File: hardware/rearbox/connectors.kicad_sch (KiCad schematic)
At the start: 2 parts, among them J3 Conn_02x28_Top_Bottom, J4 Auxiliary

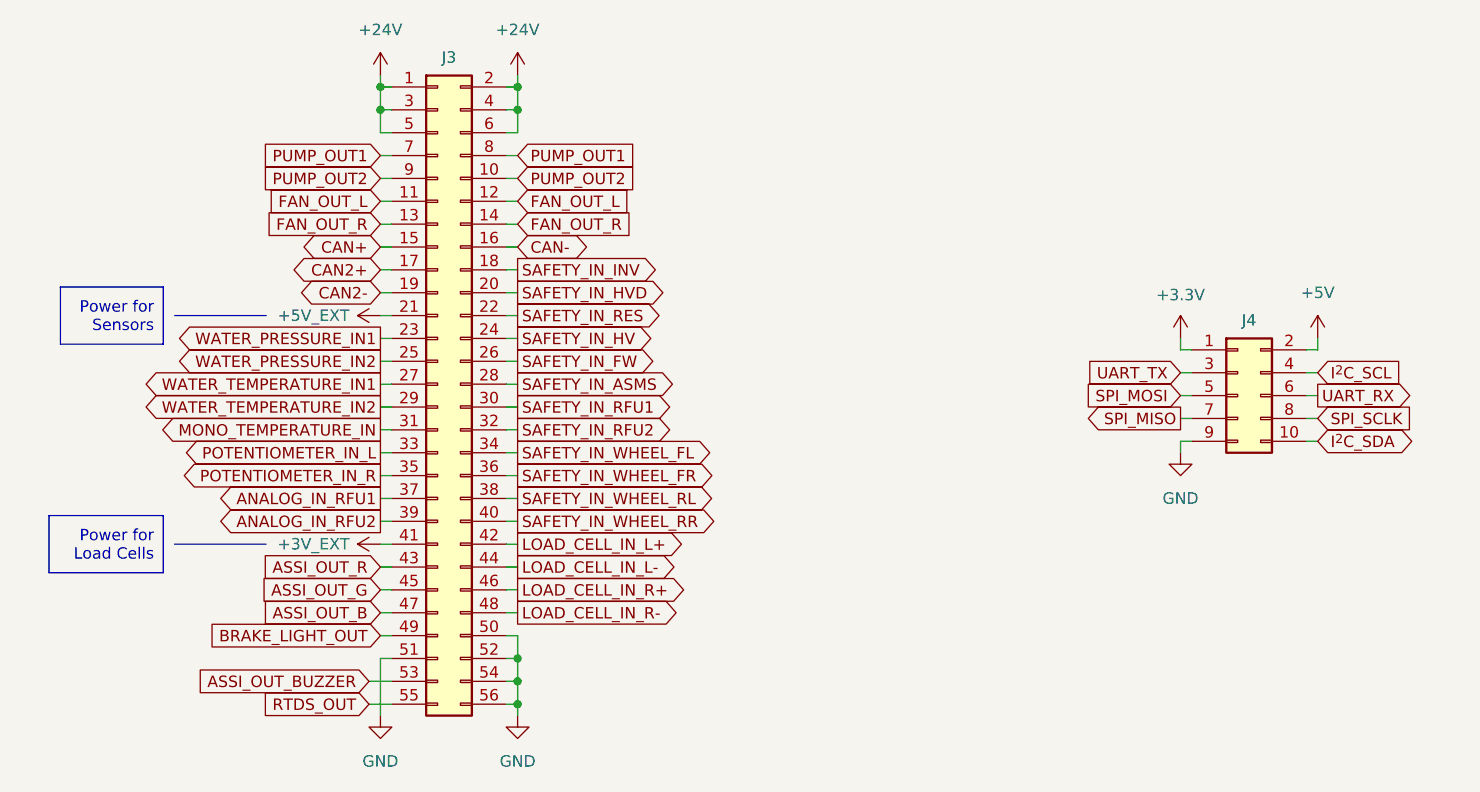
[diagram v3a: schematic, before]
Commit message: Route PCB tracks
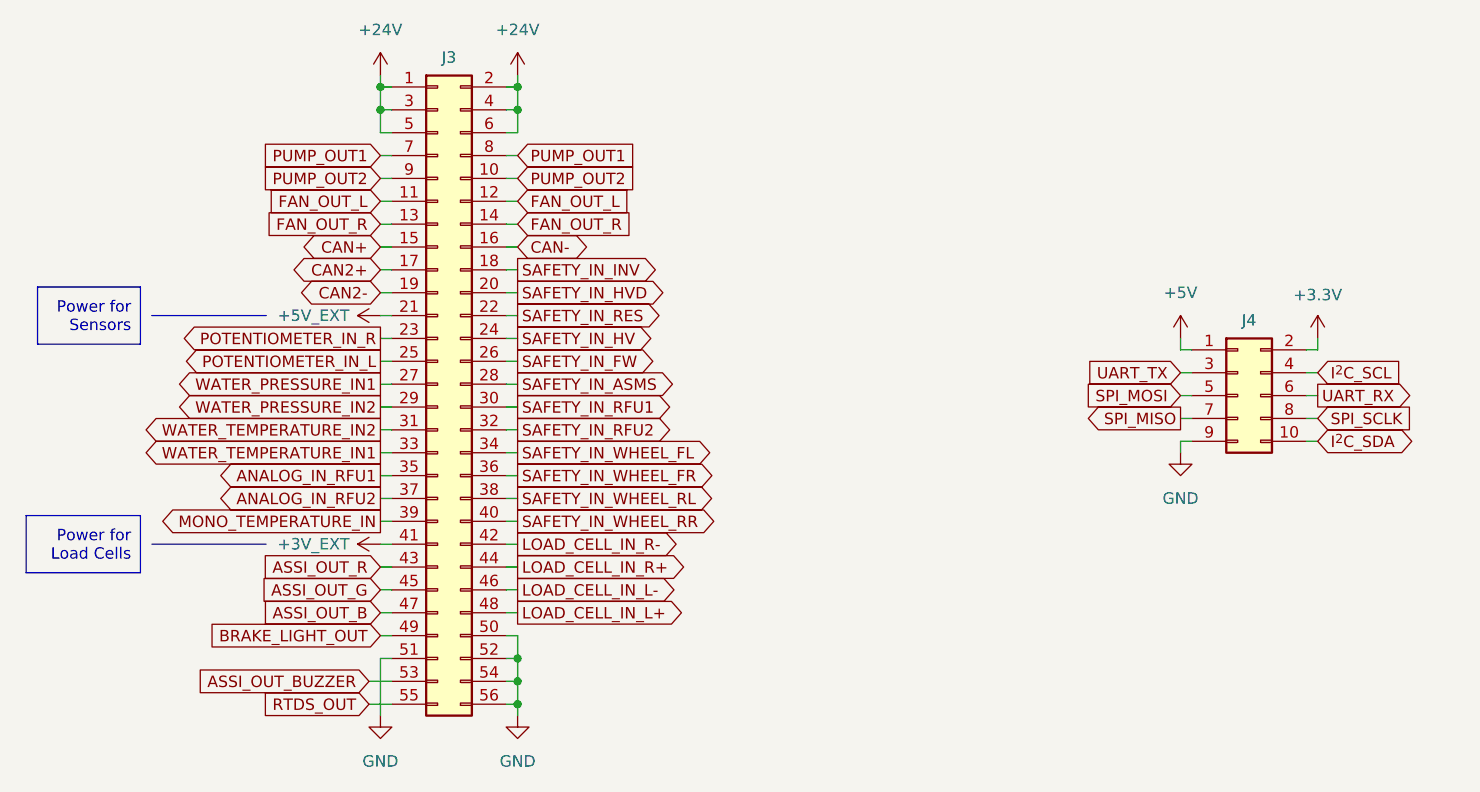
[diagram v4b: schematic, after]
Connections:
- net +3.3V: now also J4.2 (Pin_2); no longer J4.1 (Pin_1)
- net +5V: now also J4.1 (Pin_1); no longer J4.2 (Pin_2)
- net ANALOG_IN_RFU1: now also J3.35 (Pin_35); no longer J3.37 (Pin_37)
- net ANALOG_IN_RFU2: now also J3.37 (Pin_37); no longer J3.39 (Pin_39)
- net LOAD_CELL_IN_L+: now also J3.48 (Pin_48); no longer J3.42 (Pin_42)
- net LOAD_CELL_IN_L-: now also J3.46 (Pin_46); no longer J3.44 (Pin_44)
- net LOAD_CELL_IN_R+: now also J3.44 (Pin_44); no longer J3.46 (Pin_46)
- net LOAD_CELL_IN_R-: now also J3.42 (Pin_42); no longer J3.48 (Pin_48)
- net MONO_TEMPERATURE_IN: now also J3.39 (Pin_39); no longer J3.31 (Pin_31)
- net POTENTIOMETER_IN_L: now also J3.25 (Pin_25); no longer J3.33 (Pin_33)
- net POTENTIOMETER_IN_R: now also J3.23 (Pin_23); no longer J3.35 (Pin_35)
- net WATER_PRESSURE_IN1: now also J3.27 (Pin_27); no longer J3.23 (Pin_23)
- net WATER_PRESSURE_IN2: now also J3.29 (Pin_29); no longer J3.25 (Pin_25)
- net WATER_TEMPERATURE_IN1: now also J3.33 (Pin_33); no longer J3.27 (Pin_27)
- net WATER_TEMPERATURE_IN2: now also J3.31 (Pin_31); no longer J3.29 (Pin_29)
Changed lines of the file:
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@@
     (stroke (width 0) (type default))
   )
-  (polyline (pts (xy 93.98 91.44) (xy 83.82 91.44))
+  (polyline (pts (xy 93.98 91.44) (xy 81.28 91.44))
     (stroke (width 0) (type default))
   )
@@
     (stroke (width 0) (type default))
   )
-  (polyline (pts (xy 93.98 116.84) (xy 83.82 116.84))
+  (polyline (pts (xy 93.98 116.84) (xy 81.28 116.84))
     (stroke (width 0) (type default))
   )
@@
   )
   (text_box "Power for Sensors"
-    (at 71.12 88.265 0) (size 11.43 6.35)
+    (at 68.58 88.265 0) (size 11.43 6.35)
     (stroke (width 0) (type default))
     (fill (type none))
@@
   )
   (text_box "Power for Load Cells"
-    (at 69.85 113.665 0) (size 12.7 6.35)
+    (at 67.31 113.665 0) (size 12.7 6.35)
     (stroke (width 0) (type default))
     (fill (type none))
     (effects (font (size 1.27 1.27)) (justify right))
   )
-  (global_label "WATER_PRESSURE_IN1" (shape output) (at 106.68 93.98 180) (fields_autoplaced)
+  (global_label "WATER_PRESSURE_IN1" (shape output) (at 106.68 99.06 180) (fields_autoplaced)
     (effects (font (size 1.27 1.27) (color 0 132 132 1)) (justify right))
-    (property "Intersheetrefs" "${INTERSHEET_REFS}" (at 82.9101 93.98 0)
+    (property "Intersheetrefs" "${INTERSHEET_REFS}" (at 82.9101 99.06 0)
       (effects (font (size 1.27 1.27)) (justify right) hide)
     )
@@
     )
   )
-  (global_label "WATER_PRESSURE_IN2" (shape output) (at 106.68 96.52 180) (fields_autoplaced)
+  (global_label "WATER_PRESSURE_IN2" (shape output) (at 106.68 101.6 180) (fields_autoplaced)
     (effects (font (size 1.27 1.27) (color 0 132 132 1)) (justify right))
-    (property "Intersheetrefs" "${INTERSHEET_REFS}" (at 82.9101 96.52 0)
+    (property "Intersheetrefs" "${INTERSHEET_REFS}" (at 82.9101 101.6 0)
       (effects (font (size 1.27 1.27)) (justify right) hide)
     )
@@
     )
   )
-  (global_label "WATER_TEMPERATURE_IN1" (shape output) (at 106.68 99.06 180) (fields_autoplaced)
+  (global_label "WATER_TEMPERATURE_IN1" (shape output) (at 106.68 106.68 180) (fields_autoplaced)
     (effects (font (size 1.27 1.27) (color 0 255 255 1)) (justify right))
-    (property "Intersheetrefs" "${INTERSHEET_REFS}" (at 79.7049 99.06 0)
+    (property "Intersheetrefs" "${INTERSHEET_REFS}" (at 79.7049 106.68 0)
       (effects (font (size 1.27 1.27)) (justify right) hide)
     )
@@
     )
   )
-  (global_label "LOAD_CELL_IN_R+" (shape output) (at 121.92 121.92 0) (fields_autoplaced)
+  (global_label "LOAD_CELL_IN_R+" (shape output) (at 121.92 119.38 0) (fields_autoplaced)
     (effects (font (size 1.27 1.27)) (justify left))
-    (property "Intersheetrefs" "${INTERSHEET_REFS}" (at 141.7781 121.92 0)
+    (property "Intersheetrefs" "${INTERSHEET_REFS}" (at 141.7781 119.38 0)
       (effects (font (size 1.27 1.27)) (justify left) hide)
     )
@@
     )
   )
-  (global_label "LOAD_CELL_IN_R-" (shape output) (at 121.92 124.46 0) (fields_autoplaced)
+  (global_label "LOAD_CELL_IN_R-" (shape output) (at 121.92 116.84 0) (fields_autoplaced)
     (effects (font (size 1.27 1.27)) (justify left))
-    (property "Intersheetrefs" "${INTERSHEET_REFS}" (at 141.7781 124.46 0)
-      (effects (font (size 1.27 1.27)) (justify left) hide)
-    )
-  )
-  (global_label "LOAD_CELL_IN_L+" (shape output) (at 121.92 116.84 0) (fields_autoplaced)
+    (property "Intersheetrefs" "${INTERSHEET_REFS}" (at 141.7781 116.84 0)
+      (effects (font (size 1.27 1.27)) (justify left) hide)
+    )
+  )
+  (global_label "LOAD_CELL_IN_L+" (shape output) (at 121.92 124.46 0) (fields_autoplaced)
     (effects (font (size 1.27 1.27)) (justify left))
-    (property "Intersheetrefs" "${INTERSHEET_REFS}" (at 141.5362 116.84 0)
+    (property "Intersheetrefs" "${INTERSHEET_REFS}" (at 141.5362 124.46 0)
       (effects (font (size 1.27 1.27)) (justify left) hide)
     )
@@
     )
   )
-  (global_label "MONO_TEMPERATURE_IN" (shape output) (at 106.68 104.14 180) (fields_autoplaced)
+  (global_label "MONO_TEMPERATURE_IN" (shape output) (at 106.68 114.3 180) (fields_autoplaced)
     (effects (font (size 1.27 1.27) (color 0 255 255 1)) (justify right))
-    (property "Intersheetrefs" "${INTERSHEET_REFS}" (at 81.3981 104.14 0)
+    (property "Intersheetrefs" "${INTERSHEET_REFS}" (at 81.3981 114.3 0)
       (effects (font (size 1.27 1.27)) (justify right) hide)
     )
@@
     )
   )
-  (global_label "ANALOG_IN_RFU2" (shape output) (at 106.68 114.3 180) (fields_autoplaced)
+  (global_label "ANALOG_IN_RFU2" (shape output) (at 106.68 111.76 180) (fields_autoplaced)
     (effects (font (size 1.27 1.27)) (justify right))
-    (property "Intersheetrefs" "${INTERSHEET_REFS}" (at 87.7894 114.3 0)
+    (property "Intersheetrefs" "${INTERSHEET_REFS}" (at 87.7894 111.76 0)
       (effects (font (size 1.27 1.27)) (justify right) hide)
     )
@@
     )
   )
-  (global_label "LOAD_CELL_IN_L-" (shape output) (at 121.92 119.38 0) (fields_autoplaced)
+  (global_label "LOAD_CELL_IN_L-" (shape output) (at 121.92 121.92 0) (fields_autoplaced)
     (effects (font (size 1.27 1.27)) (justify left))
-    (property "Intersheetrefs" "${INTERSHEET_REFS}" (at 141.5362 119.38 0)
+    (property "Intersheetrefs" "${INTERSHEET_REFS}" (at 141.5362 121.92 0)
       (effects (font (size 1.27 1.27)) (justify left) hide)
     )
@@
     )
   )
-  (global_label "POTENTIOMETER_IN_R" (shape output) (at 106.68 109.22 180) (fields_autoplaced)
+  (global_label "POTENTIOMETER_IN_R" (shape output) (at 106.68 93.98 180) (fields_autoplaced)
     (effects (font (size 1.27 1.27)) (justify right))
-    (property "Intersheetrefs" "${INTERSHEET_REFS}" (at 83.6168 109.22 0)
-      (effects (font (size 1.27 1.27)) (justify right) hide)
-    )
-  )
-  (global_label "ANALOG_IN_RFU1" (shape output) (at 106.68 111.76 180) (fields_autoplaced)
+    (property "Intersheetrefs" "${INTERSHEET_REFS}" (at 83.6168 93.98 0)
+      (effects (font (size 1.27 1.27)) (justify right) hide)
+    )
+  )
+  (global_label "ANALOG_IN_RFU1" (shape output) (at 106.68 109.22 180) (fields_autoplaced)
     (effects (font (size 1.27 1.27)) (justify right))
-    (property "Intersheetrefs" "${INTERSHEET_REFS}" (at 87.7894 111.76 0)
-      (effects (font (size 1.27 1.27)) (justify right) hide)
-    )
-  )
-  (global_label "POTENTIOMETER_IN_L" (shape output) (at 106.68 106.68 180) (fields_autoplaced)
+    (property "Intersheetrefs" "${INTERSHEET_REFS}" (at 87.7894 109.22 0)
+      (effects (font (size 1.27 1.27)) (justify right) hide)
+    )
+  )
+  (global_label "POTENTIOMETER_IN_L" (shape output) (at 106.68 96.52 180) (fields_autoplaced)
     (effects (font (size 1.27 1.27)) (justify right))
-    (property "Intersheetrefs" "${INTERSHEET_REFS}" (at 83.8587 106.68 0)
+    (property "Intersheetrefs" "${INTERSHEET_REFS}" (at 83.8587 96.52 0)
       (effects (font (size 1.27 1.27)) (justify right) hide)
     )
@@
     )
   )
-  (global_label "WATER_TEMPERATURE_IN2" (shape output) (at 106.68 101.6 180) (fields_autoplaced)
+  (global_label "WATER_TEMPERATURE_IN2" (shape output) (at 106.68 104.14 180) (fields_autoplaced)
     (effects (font (size 1.27 1.27) (color 0 255 255 1)) (justify right))
-    (property "Intersheetrefs" "${INTERSHEET_REFS}" (at 79.7049 101.6 0)
+    (property "Intersheetrefs" "${INTERSHEET_REFS}" (at 79.7049 104.14 0)
       (effects (font (size 1.27 1.27)) (justify right) hide)
     )
@@
     )
   )
-  (symbol (lib_id "power:+5V") (at 210.82 93.98 0) (unit 1)
+  (symbol (lib_id "power:+5V") (at 195.58 93.98 0) (unit 1)
     (in_bom yes) (on_board yes) (dnp no)
-    (property "Reference" "#PWR037" (at 210.82 97.79 0)
-      (effects (font (size 1.27 1.27)) hide)
-    )
-    (property "Value" "+5V" (at 210.82 88.9 0)
+    (property "Reference" "#PWR037" (at 195.58 97.79 0)
+      (effects (font (size 1.27 1.27)) hide)
+    )
+    (property "Value" "+5V" (at 195.58 88.9 0)
       (effects (font (size 1.27 1.27)))
     )
-    (property "Footprint" "" (at 210.82 93.98 0)
-      (effects (font (size 1.27 1.27)) hide)
-    )
-    (property "Datasheet" "" (at 210.82 93.98 0)
+    (property "Footprint" "" (at 195.58 93.98 0)
+      (effects (font (size 1.27 1.27)) hide)
+    )
+    (property "Datasheet" "" (at 195.58 93.98 0)
       (effects (font (size 1.27 1.27)) hide)
     )
@@
     )
   )
-  (symbol (lib_id "power:+3.3V") (at 195.58 93.98 0) (unit 1)
+  (symbol (lib_id "power:+3.3V") (at 210.82 93.98 0) (unit 1)
     (in_bom yes) (on_board yes) (dnp no)
-    (property "Reference" "#PWR016" (at 195.58 97.79 0)
-      (effects (font (size 1.27 1.27)) hide)
-    )
-    (property "Value" "+3.3V" (at 195.58 89.154 0)
+    (property "Reference" "#PWR016" (at 210.82 97.79 0)
+      (effects (font (size 1.27 1.27)) hide)
+    )
+    (property "Value" "+3.3V" (at 210.82 89.154 0)
       (effects (font (size 1.27 1.27)))
     )
-    (property "Footprint" "" (at 195.58 93.98 0)
-      (effects (font (size 1.27 1.27)) hide)
-    )
-    (property "Datasheet" "" (at 195.58 93.98 0)
-      (effects (font (size 1.27 1.27)) hide)
-    )
+    (property "Footprint" "" (at 210.82 93.98 0)
+      (effects (font (size 1.27 1.27)) hide)
+    )
+    (property "Datasheet" "" (at 210.82 93.98 0)
+      (effects (font (size 1.27 1.27)) hide)
+    )

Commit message: Fix DRCs
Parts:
- J3: footprint Connector_PinHeader_2.00mm:PinHeader_2x28_P2.00mm_Horizontal -> Local_Library:PinHeader_2x28_P2.00mm_Horizontal
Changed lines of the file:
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@@
   (title_block
     (title "Connectors")
-    (date "2023-11-02")
+    (date "2023-11-17")
     (rev "${REVISION}")
     (company "Author: I. Kajdan")
@@
         )
         (path "/b652b05a-4e3d-4ad1-b032-18886abe7d45/cf65c657-8245-46fb-8929-d241bd579513"
-          (reference "#PWR058") (unit 1)
+          (reference "#PWR056") (unit 1)
         )
       )
@@
         )
         (path "/b652b05a-4e3d-4ad1-b032-18886abe7d45/cf65c657-8245-46fb-8929-d241bd579513"
-          (reference "#PWR056") (unit 1)
+          (reference "#PWR058") (unit 1)
         )
       )
@@
       (effects (font (size 1.27 1.27)) hide)
     )
-    (property "Footprint" "Connector_PinHeader_2.00mm:PinHeader_2x28_P2.00mm_Horizontal" (at 113.03 99.06 0)
-      (effects (font (size 1.27 1.27)) hide)
-    )
+    (property "Footprint" "Local_Library:PinHeader_2x28_P2.00mm_Horizontal" (at 113.03 99.06 0)
+      (effects (font (size 1.27 1.27)) hide)
+    )

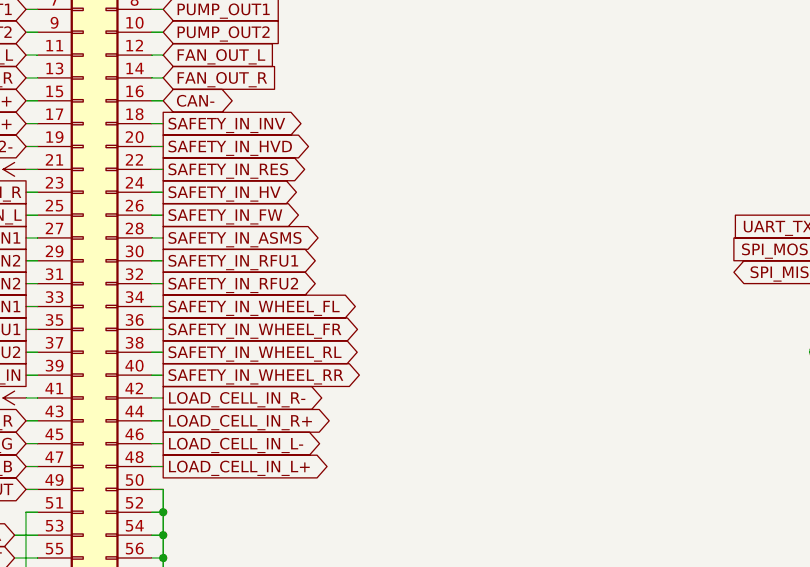
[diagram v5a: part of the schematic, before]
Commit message: Route the tracks on the connector PCB
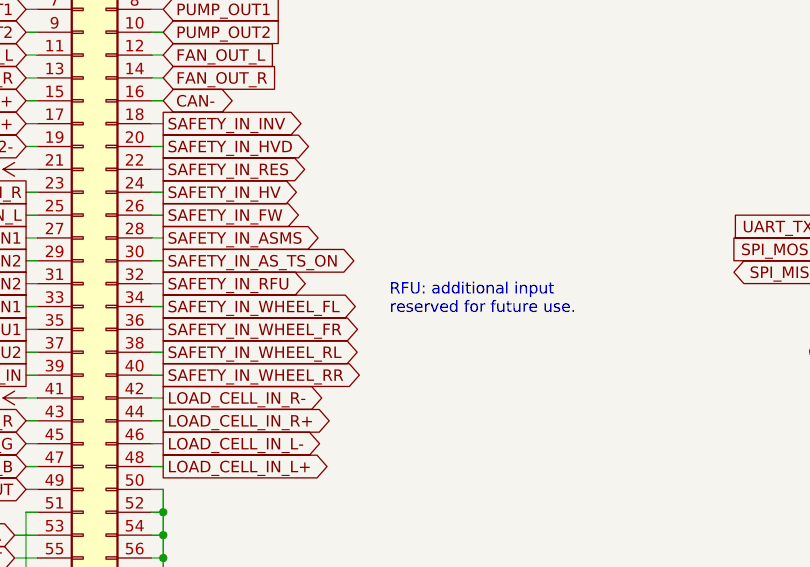
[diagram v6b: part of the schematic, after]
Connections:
- net SAFETY_IN_RFU1 renamed SAFETY_IN_AS_TS_ON
- net SAFETY_IN_RFU2 renamed SAFETY_IN_RFU
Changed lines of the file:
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@@
     (effects (font (size 1.27 1.27)) (justify right))
+  )
+  (text_box "RFU: additional input reserved for future use."
+    (at 146.05 102.87 0) (size 29.21 5.08)
+    (stroke (width -0.0001) (type default))
+    (fill (type none))
+    (effects (font (size 1.27 1.27)) (justify left top))
   )
   (global_label "WATER_PRESSURE_IN1" (shape output) (at 106.68 99.06 180) (fields_autoplaced)
@@
     )
   )
-  (global_label "SAFETY_IN_RFU2" (shape output) (at 121.92 104.14 0) (fields_autoplaced)
-    (effects (font (size 1.27 1.27) (color 179 0 27 1)) (justify left))
-    (property "Intersheetrefs" "${INTERSHEET_REFS}" (at 140.1868 104.14 0)
+  (global_label "SAFETY_IN_RFU" (shape output) (at 121.92 104.14 0) (fields_autoplaced)
+    (effects (font (size 1.27 1.27) (color 179 0 27 1)) (justify left))
+    (property "Intersheetrefs" "${INTERSHEET_REFS}" (at 139.0567 104.14 0)
       (effects (font (size 1.27 1.27)) (justify left) hide)
     )
@@
     )
   )
-  (global_label "SAFETY_IN_RFU1" (shape output) (at 121.92 101.6 0) (fields_autoplaced)
-    (effects (font (size 1.27 1.27) (color 179 0 27 1)) (justify left))
-    (property "Intersheetrefs" "${INTERSHEET_REFS}" (at 140.1868 101.6 0)
+  (global_label "SAFETY_IN_AS_TS_ON" (shape output) (at 121.92 101.6 0) (fields_autoplaced)
+    (effects (font (size 1.27 1.27) (color 179 0 27 1)) (justify left))
+    (property "Intersheetrefs" "${INTERSHEET_REFS}" (at 144.439 101.6 0)
       (effects (font (size 1.27 1.27)) (justify left) hide)
     )
@@
   (symbol (lib_id "power:+5V") (at 195.58 93.98 0) (unit 1)
     (in_bom yes) (on_board yes) (dnp no)
-    (property "Reference" "#PWR037" (at 195.58 97.79 0)
+    (property "Reference" "#PWR056" (at 195.58 97.79 0)
       (effects (font (size 1.27 1.27)) hide)
     )
@@
     (instances
       (project "rearbox"
-        (path "/b652b05a-4e3d-4ad1-b032-18886abe7d45/7045152e-d7a2-42d7-9b15-138e7f2928ca"
-          (reference "#PWR037") (unit 1)
-        )
         (path "/b652b05a-4e3d-4ad1-b032-18886abe7d45/cf65c657-8245-46fb-8929-d241bd579513"
           (reference "#PWR056") (unit 1)
@@
   (symbol (lib_id "power:+3.3V") (at 210.82 93.98 0) (unit 1)
     (in_bom yes) (on_board yes) (dnp no)
-    (property "Reference" "#PWR016" (at 210.82 97.79 0)
+    (property "Reference" "#PWR058" (at 210.82 97.79 0)
       (effects (font (size 1.27 1.27)) hide)
     )
@@
     (instances
       (project "rearbox"
-        (path "/b652b05a-4e3d-4ad1-b032-18886abe7d45"
-          (reference "#PWR016") (unit 1)
-        )
         (path "/b652b05a-4e3d-4ad1-b032-18886abe7d45/cf65c657-8245-46fb-8929-d241bd579513"
           (reference "#PWR058") (unit 1)
